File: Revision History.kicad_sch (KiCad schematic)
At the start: 0 parts

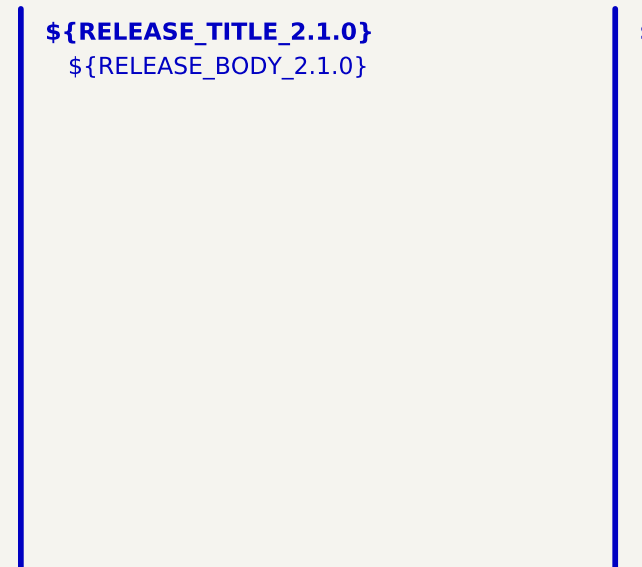
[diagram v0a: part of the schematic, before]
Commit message: documentation update / release 2.1.1 prep
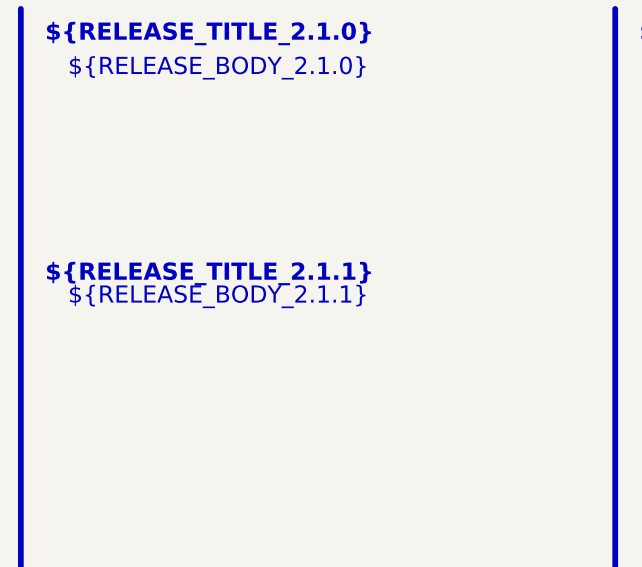
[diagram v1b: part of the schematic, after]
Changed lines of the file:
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@@
 		(company "${COMPANY}")
+	)
+	(text_box "${RELEASE_TITLE_2.1.1}"
+		(exclude_from_sim no)
+		(at 20.32 58.42 0)
+		(size 57.15 7.62)
+		(margins 1.4287 1.4287 1.4287 1.4287)
+		(stroke
+			(width -0.0001)
+			(type solid)
+		)
+		(fill
+			(type none)
+		)
+		(effects
+			(font
+				(face "Arial")
+				(size 1.905 1.905)
+				(thickness 0.254)
+				(bold yes)
+			)
+			(justify left top)
+		)
 	)
 	(text_box "${RELEASE_BODY_1.1.0}"
@@
 		(exclude_from_sim no)
 		(at 22.86 35.56 0)
-		(size 58.42 146.05)
+		(size 58.42 21.59)
 		(margins 1.4287 1.4287 1.4287 1.4287)
 		(stroke
@@
 			)
 			(justify left top)
+		)
+	)
+	(text_box "${RELEASE_BODY_2.1.1}"
+		(exclude_from_sim no)
+		(at 22.86 60.96 0)
+		(size 58.42 21.59)
+		(margins 1.4287 1.4287 1.4287 1.4287)
+		(stroke
+			(width -0.0001)
+			(type solid)
+		)
+		(fill
+			(type none)
+		)
+		(effects
+			(font
+				(face "Arial")
+				(size 1.905 1.905)
+				(color 0 0 0 1)
+			)
+			(justify left top)
